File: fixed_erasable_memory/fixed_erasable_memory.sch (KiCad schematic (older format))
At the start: 1 part, among them P1 DIN_41612_128P

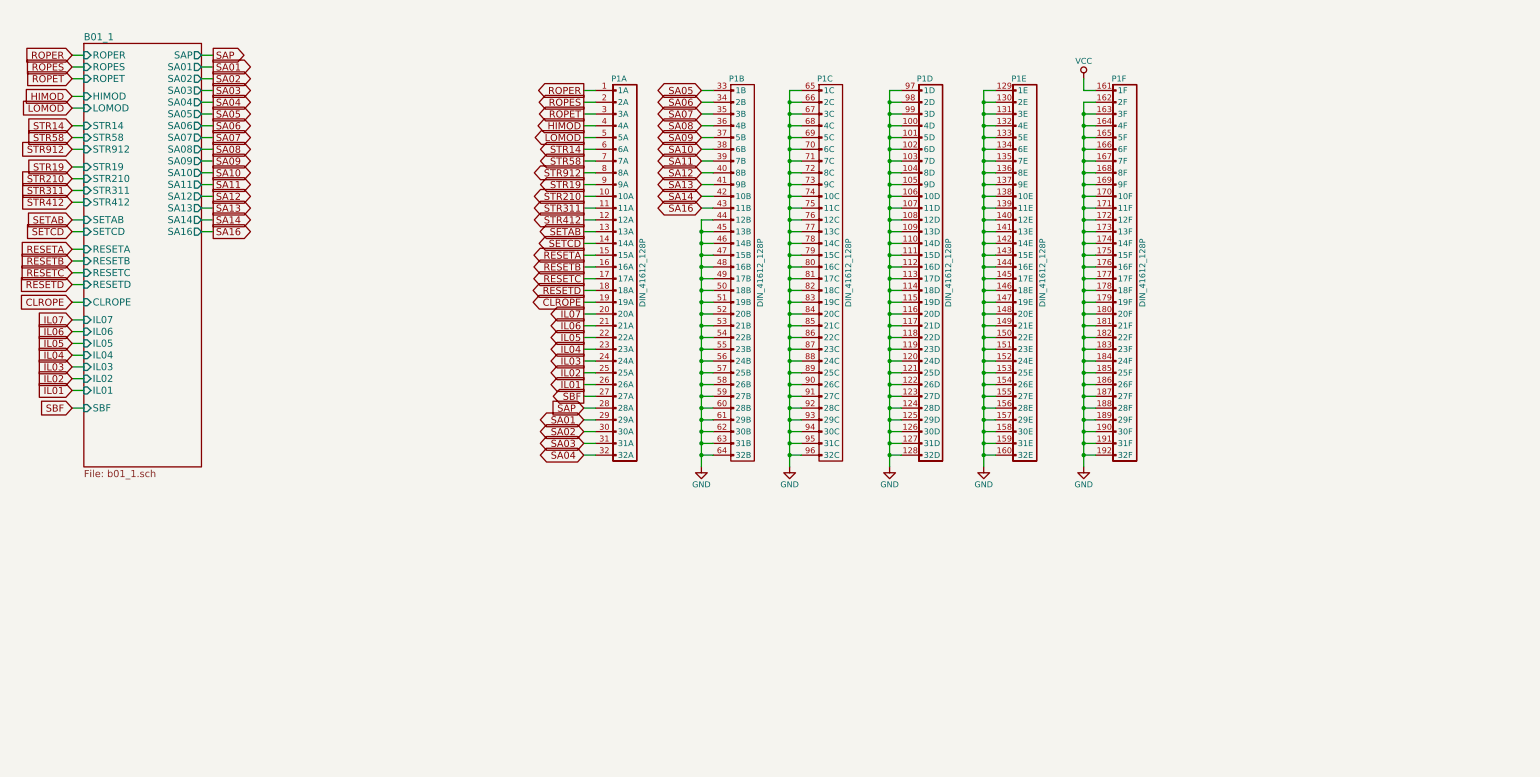
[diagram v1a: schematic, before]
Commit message: Added erasable memory, and fixed lots of random wiring errors.
I decided to go with a 16-bit-wide MRAM chip -- I had  no idea
until I started researching RAM options how technologically
similar MRAM is to core memory. The datasheet diagrams look like
they're straight out of the AGC documentation!

There's a slight inaccuracy in this implementation worth mentioning.
Like fixed memory, I've wired the sense amplifier outputs directly up
to the tristate data output pins of the MRAM chip. But because the
data lines are bidirectional, data being written into RAM will show up
on the sense lines, and go straight into the ungated G register. Since
G is what's being written out, this doesn't matter 99% of the time, but
if there's an overflow condition in G (I don't even know if this is
possible), the bit 16 will be copied over bit 16, and the overflow
condition will be lost. I'll keep an eye out to see if anything relies
on G not changing after the write cycle is complete.

With erasable memory introduced, the computer now theoretically supports
all programs that don't use I/O or interrupts. I've started running
the VirtualAGC validation program, and have been fixing random errors
uncovered by failing self-tests.
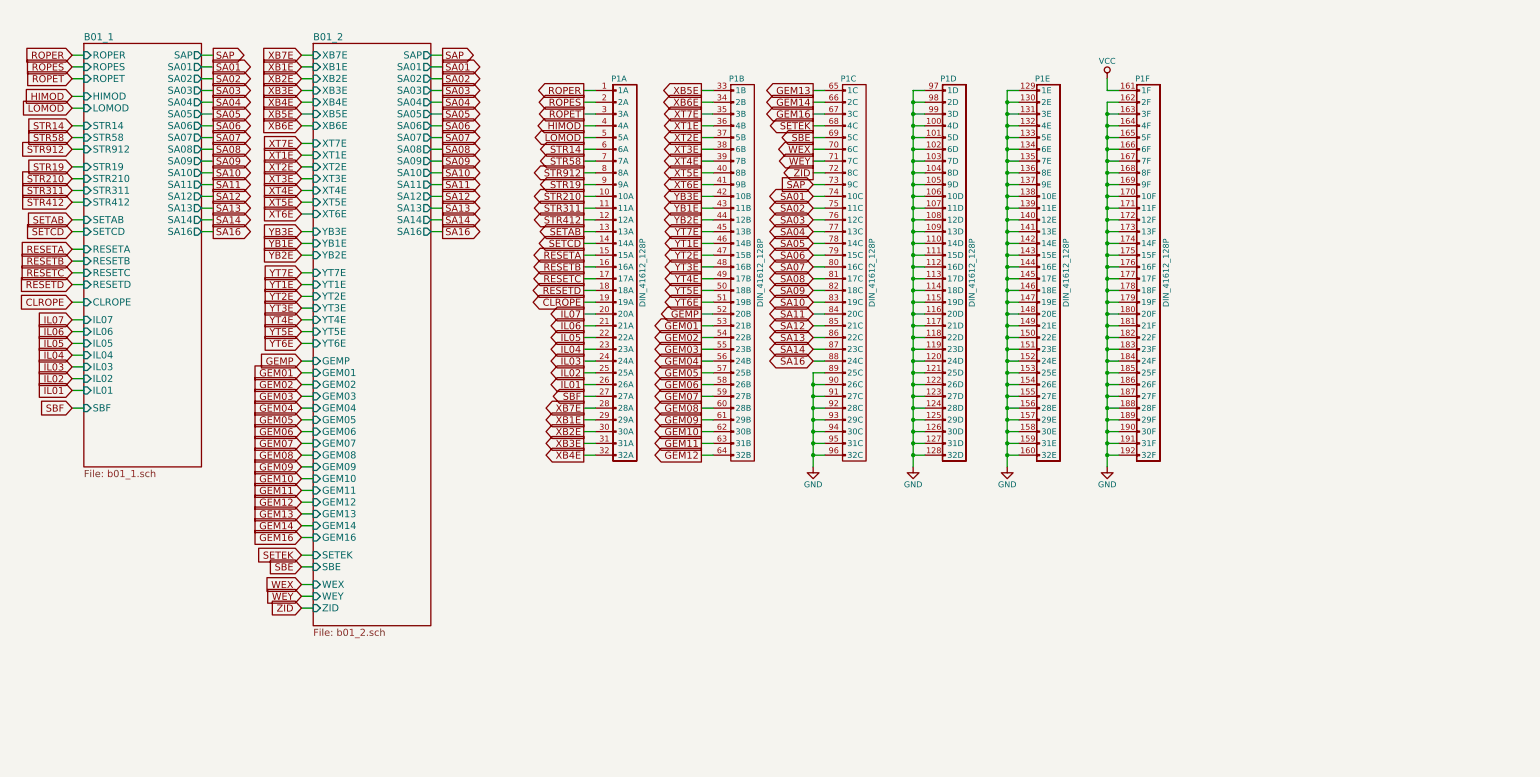
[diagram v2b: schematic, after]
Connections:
- net GND: no longer P1.44 (12B), P1.45 (13B), P1.46 (14B), P1.47 (15B), P1.48 (16B), P1.49 (17B), P1.50 (18B), P1.51 (19B), P1.52 (20B), P1.53 (21B), P1.54 (22B), P1.55 (23B), P1.56 (24B), P1.57 (25B), P1.58 (26B), P1.59 (27B), P1.60 (28B), P1.61 (29B), P1.62 (30B), P1.63 (31B), P1.64 (32B), P1.65 (1C), P1.66 (2C), P1.67 (3C), P1.68 (4C), P1.69 (5C), P1.70 (6C), P1.71 (7C), P1.72 (8C), P1.73 (9C), P1.74 (10C), P1.75 (11C), P1.76 (12C), P1.77 (13C), P1.78 (14C), P1.79 (15C), P1.80 (16C), P1.81 (17C), P1.82 (18C), P1.83 (19C), P1.84 (20C), P1.85 (21C), P1.86 (22C), P1.87 (23C), P1.88 (24C)
- net SA01: now also P1.74 (10C); no longer P1.29 (29A)
- net SA02: now also P1.75 (11C); no longer P1.30 (30A)
- net SA03: now also P1.76 (12C); no longer P1.31 (31A)
- net SA04: now also P1.77 (13C); no longer P1.32 (32A)
- net SA05: now also P1.78 (14C); no longer P1.33 (1B)
- net SA06: now also P1.79 (15C); no longer P1.34 (2B)
- net SA07: now also P1.80 (16C); no longer P1.35 (3B)
- net SA08: now also P1.81 (17C); no longer P1.36 (4B)
- net SA09: now also P1.82 (18C); no longer P1.37 (5B)
- net SA10: now also P1.83 (19C); no longer P1.38 (6B)
- net SA11: now also P1.84 (20C); no longer P1.39 (7B)
- net SA12: now also P1.85 (21C); no longer P1.40 (8B)
- net SA13: now also P1.86 (22C); no longer P1.41 (9B)
- net SA14: now also P1.87 (23C); no longer P1.42 (10B)
- net SA16: now also P1.88 (24C); no longer P1.43 (11B)
- net SAP: now also P1.73 (9C); no longer P1.28 (28A)
- new net GEM01: P1.53 (21B)
- new net GEM02: P1.54 (22B)
- new net GEM03: P1.55 (23B)
- new net GEM04: P1.56 (24B)
- new net GEM05: P1.57 (25B)
- new net GEM06: P1.58 (26B)
- new net GEM07: P1.59 (27B)
- new net GEM08: P1.60 (28B)
- new net GEM09: P1.61 (29B)
- new net GEM10: P1.62 (30B)
- new net GEM11: P1.63 (31B)
- new net GEM12: P1.64 (32B)
- new net GEM13: P1.65 (1C)
- new net GEM14: P1.66 (2C)
- new net GEM16: P1.67 (3C)
- new net GEMP: P1.52 (20B)
- new net SBE: P1.69 (5C)
- new net SETEK: P1.68 (4C)
- new net WEX: P1.70 (6C)
- new net WEY: P1.71 (7C)
- new net XB1E: P1.29 (29A)
- new net XB2E: P1.30 (30A)
- new net XB3E: P1.31 (31A)
- new net XB4E: P1.32 (32A)
- new net XB5E: P1.33 (1B)
- new net XB6E: P1.34 (2B)
- new net XB7E: P1.28 (28A)
- new net XT1E: P1.36 (4B)
- new net XT2E: P1.37 (5B)
- new net XT3E: P1.38 (6B)
- new net XT4E: P1.39 (7B)
- new net XT5E: P1.40 (8B)
- new net XT6E: P1.41 (9B)
- new net XT7E: P1.35 (3B)
- new net YB1E: P1.43 (11B)
- new net YB2E: P1.44 (12B)
- new net YB3E: P1.42 (10B)
- new net YT1E: P1.46 (14B)
- new net YT2E: P1.47 (15B)
- new net YT3E: P1.48 (16B)
- new net YT4E: P1.49 (17B)
- new net YT5E: P1.50 (18B)
- new net YT6E: P1.51 (19B)
- new net YT7E: P1.45 (13B)
- new net ZID: P1.72 (8C)
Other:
- moved on the sheet: P1C, P1D, P1E, P1F
